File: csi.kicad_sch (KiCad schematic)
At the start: 61 parts, among them J10 Conn_FFC_WE_68715014522, J11 Conn_FFC_WE_68715014522, U43 PI4MSD5V9548AZDEX, U44 AP22615A_TSOT26, U45 AP22615A_TSOT26, U46 AP22615A_TSOT26, U47 AP22615A_TSOT26, U48 NTS0102_XSON, U49 NTS0102_XSON

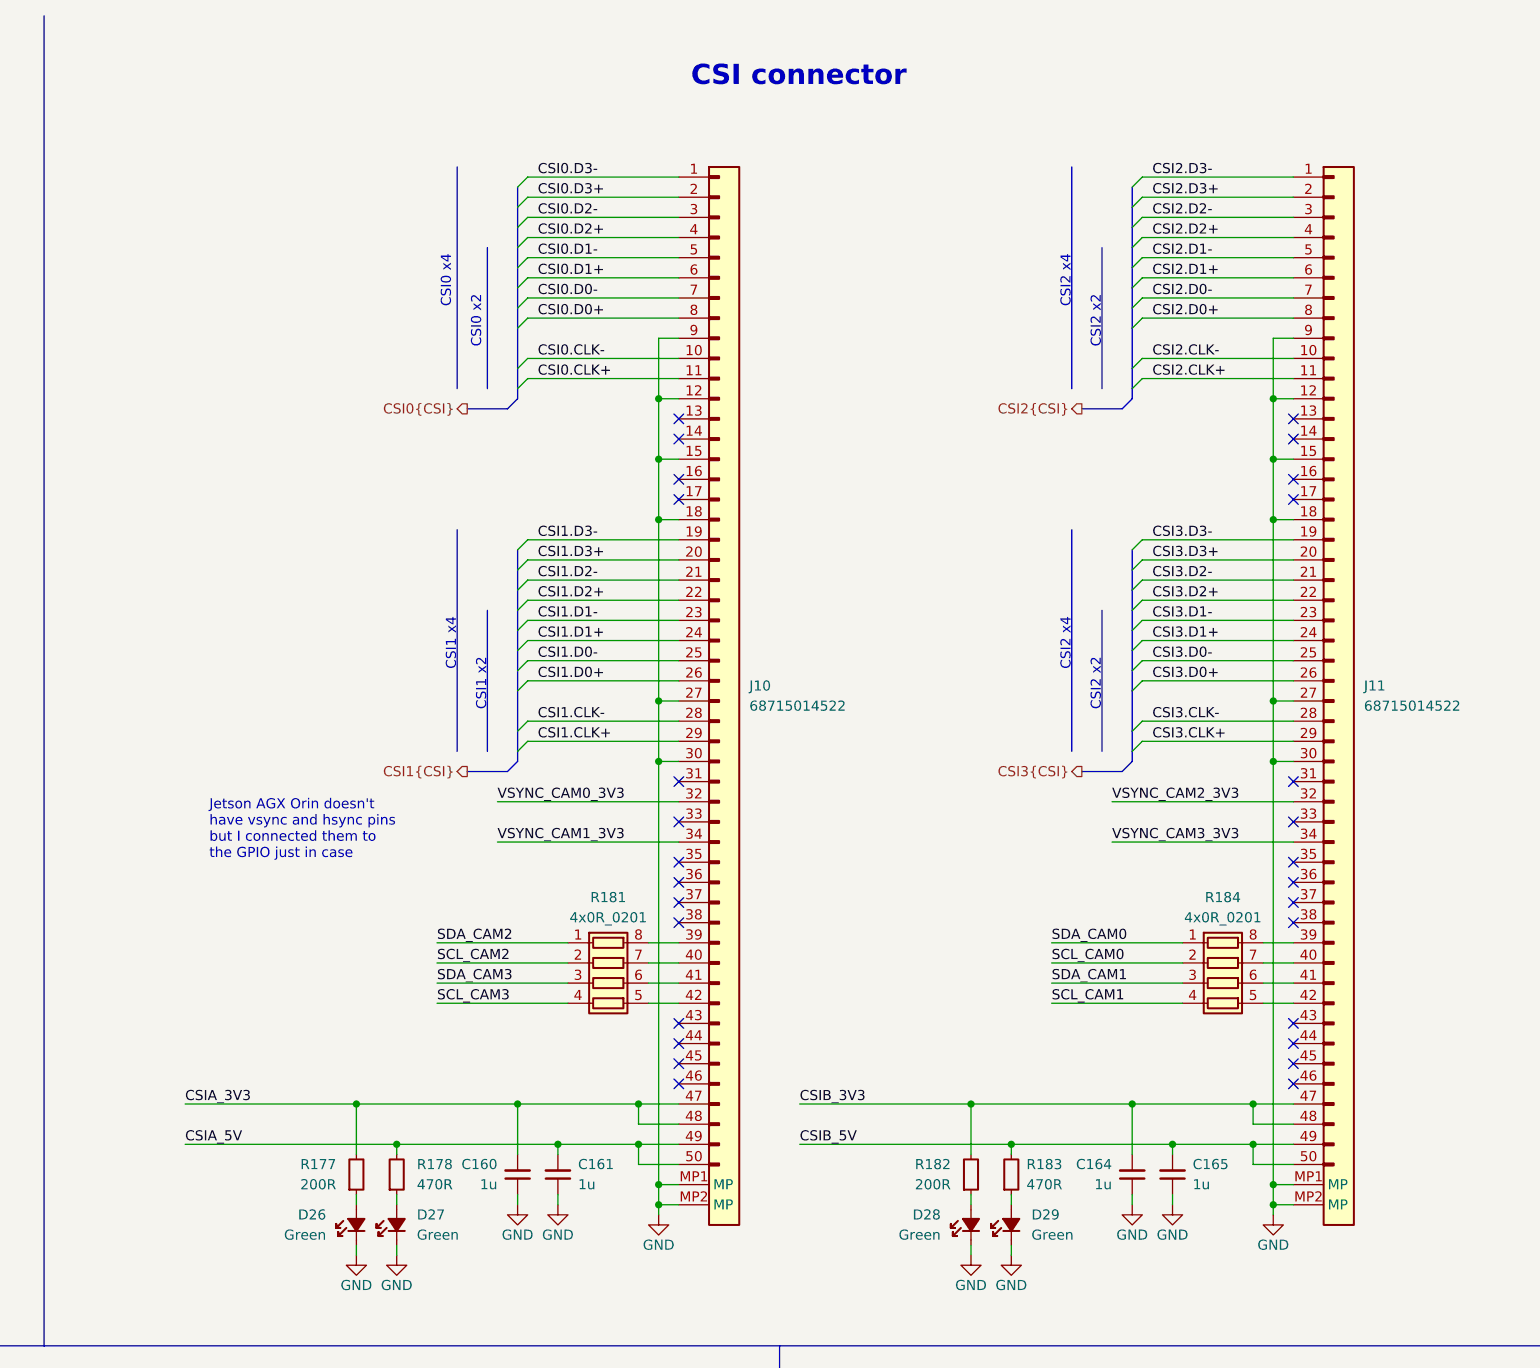
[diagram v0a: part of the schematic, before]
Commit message: [#83396] WIP: Route CSI - SoM to J11 connector
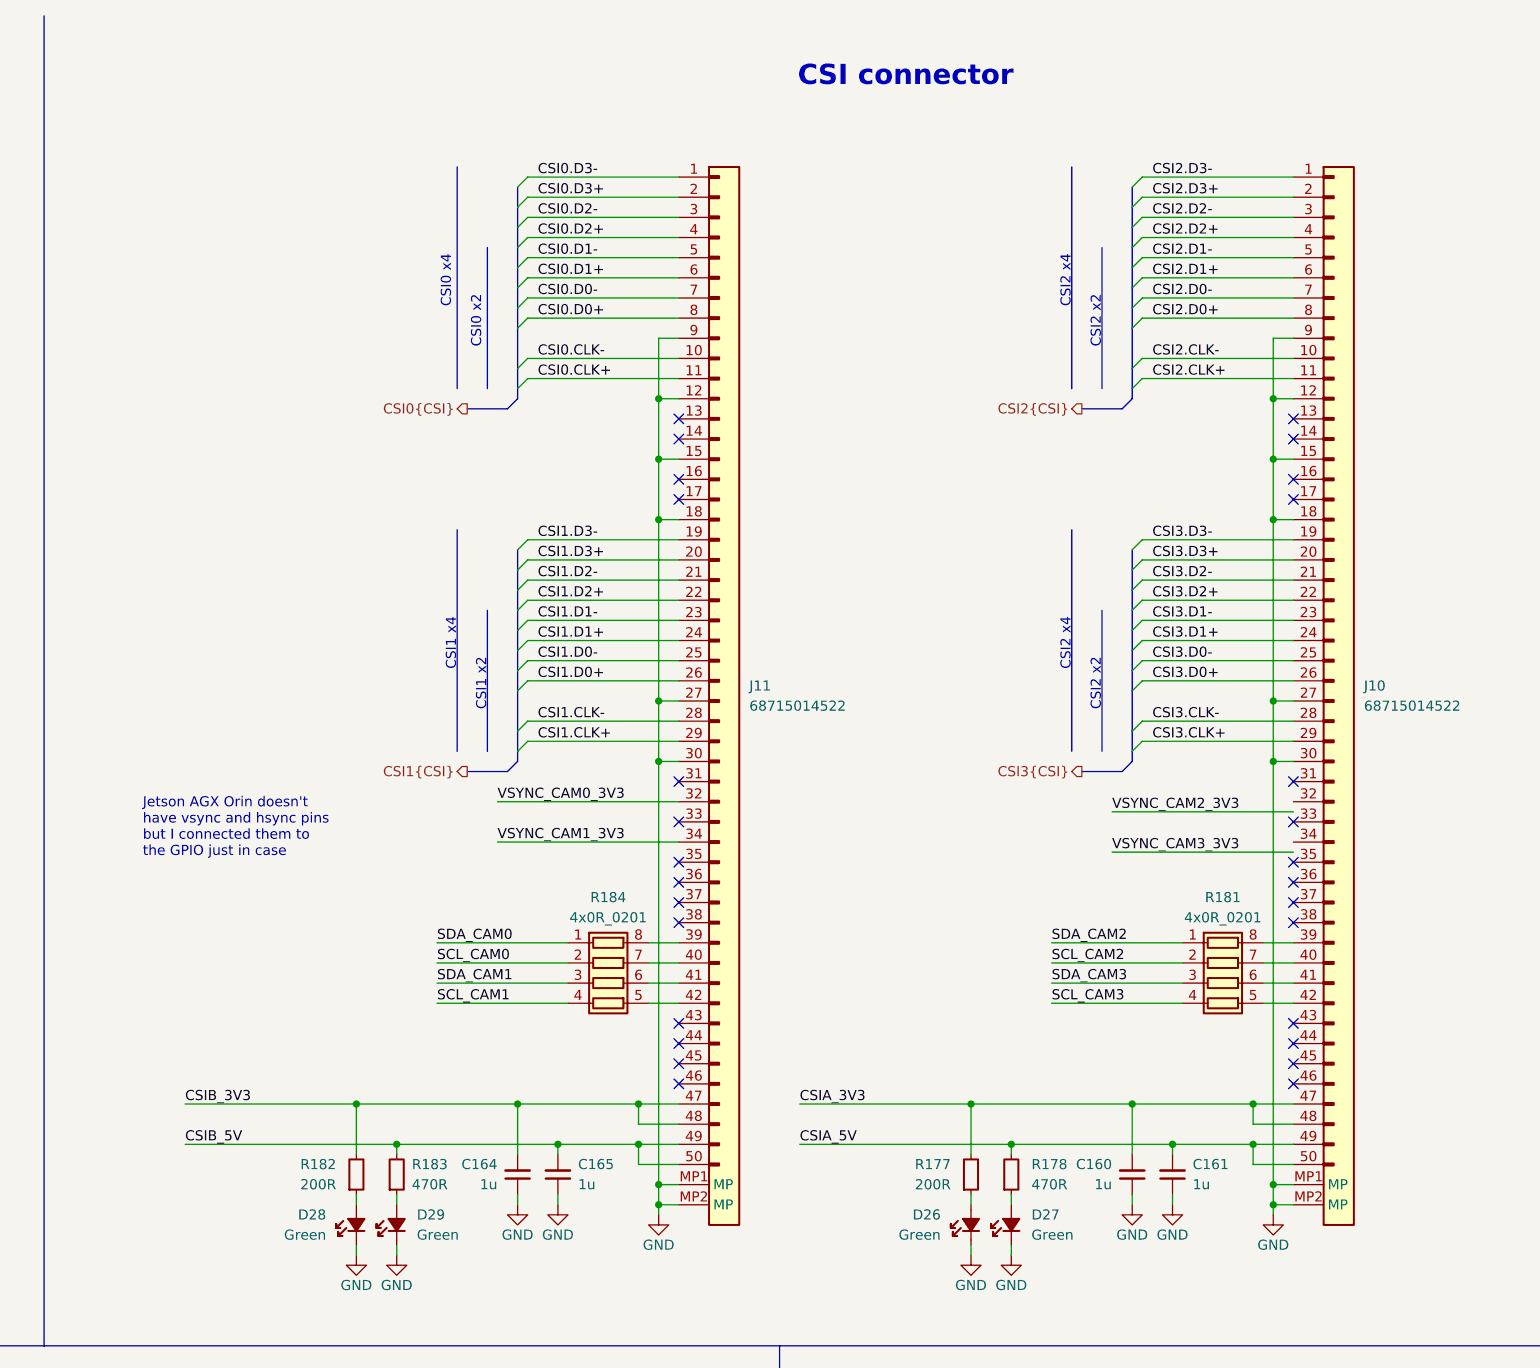
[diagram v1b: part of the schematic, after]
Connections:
- net CSI0.CLK+: now also J11.11; no longer J10.11
- net CSI0.CLK-: now also J11.10; no longer J10.10
- net CSI0.D0+: now also J11.8; no longer J10.8
- net CSI0.D0-: now also J11.7; no longer J10.7
- net CSI0.D1+: now also J11.6; no longer J10.6
- net CSI0.D1-: now also J11.5; no longer J10.5
- net CSI0.D2+: now also J11.4; no longer J10.4
- net CSI0.D2-: now also J11.3; no longer J10.3
- net CSI0.D3+: now also J11.2; no longer J10.2
- net CSI0.D3-: now also J11.1; no longer J10.1
- net CSI1.CLK+: now also J11.29; no longer J10.29
- net CSI1.CLK-: now also J11.28; no longer J10.28
- net CSI1.D0+: now also J11.26; no longer J10.26
- net CSI1.D0-: now also J11.25; no longer J10.25
- net CSI1.D1+: now also J11.24; no longer J10.24
- net CSI1.D1-: now also J11.23; no longer J10.23
- net CSI1.D2+: now also J11.22; no longer J10.22
- net CSI1.D2-: now also J11.21; no longer J10.21
- net CSI1.D3+: now also J11.20; no longer J10.20
- net CSI1.D3-: now also J11.19; no longer J10.19
- net CSI2.CLK+: now also J10.11; no longer J11.11
- net CSI2.CLK-: now also J10.10; no longer J11.10
- net CSI2.D0+: now also J10.8; no longer J11.8
- net CSI2.D0-: now also J10.7; no longer J11.7
- net CSI2.D1+: now also J10.6; no longer J11.6
- net CSI2.D1-: now also J10.5; no longer J11.5
- net CSI2.D2+: now also J10.4; no longer J11.4
- net CSI2.D2-: now also J10.3; no longer J11.3
- net CSI2.D3+: now also J10.2; no longer J11.2
- net CSI2.D3-: now also J10.1; no longer J11.1
- net CSI3.CLK+: now also J10.29; no longer J11.29
- net CSI3.CLK-: now also J10.28; no longer J11.28
- net CSI3.D0+: now also J10.26; no longer J11.26
- net CSI3.D0-: now also J10.25; no longer J11.25
- net CSI3.D1+: now also J10.24; no longer J11.24
- net CSI3.D1-: now also J10.23; no longer J11.23
- net CSI3.D2+: now also J10.22; no longer J11.22
- net CSI3.D2-: now also J10.21; no longer J11.21
- net CSI3.D3+: now also J10.20; no longer J11.20
- net CSI3.D3-: now also J10.19; no longer J11.19
- net VSYNC_CAM0_3V3: now also J11.32; no longer J10.32
- net VSYNC_CAM1_3V3: now also J11.34; no longer J10.34
- net VSYNC_CAM2_3V3: no longer J11.32
- net VSYNC_CAM3_3V3: no longer J11.34
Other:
- moved on the sheet: C160, C161, C164, C165, D26, D27, D28, D29, J10, J11, R177, R178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

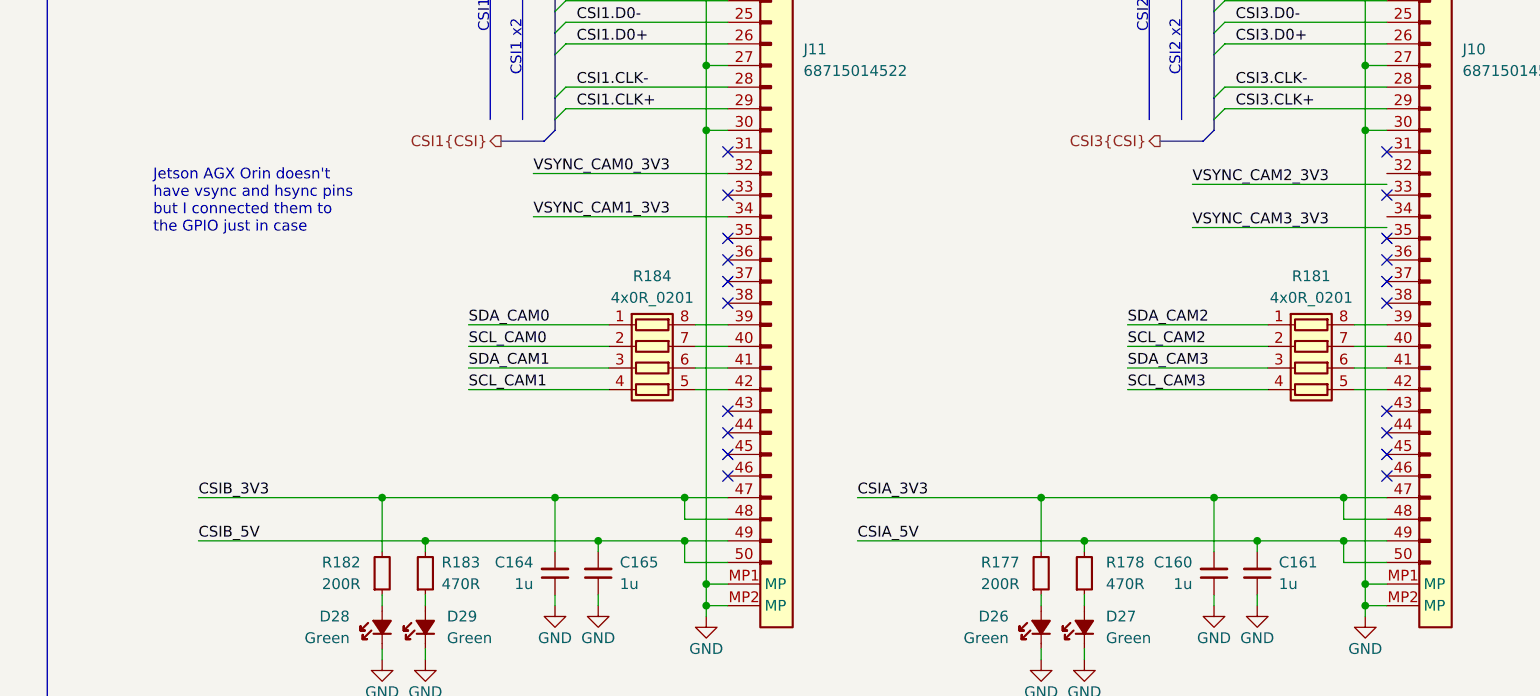
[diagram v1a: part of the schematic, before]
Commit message: [#83396] Update all symbols from library and clear all ERC errors
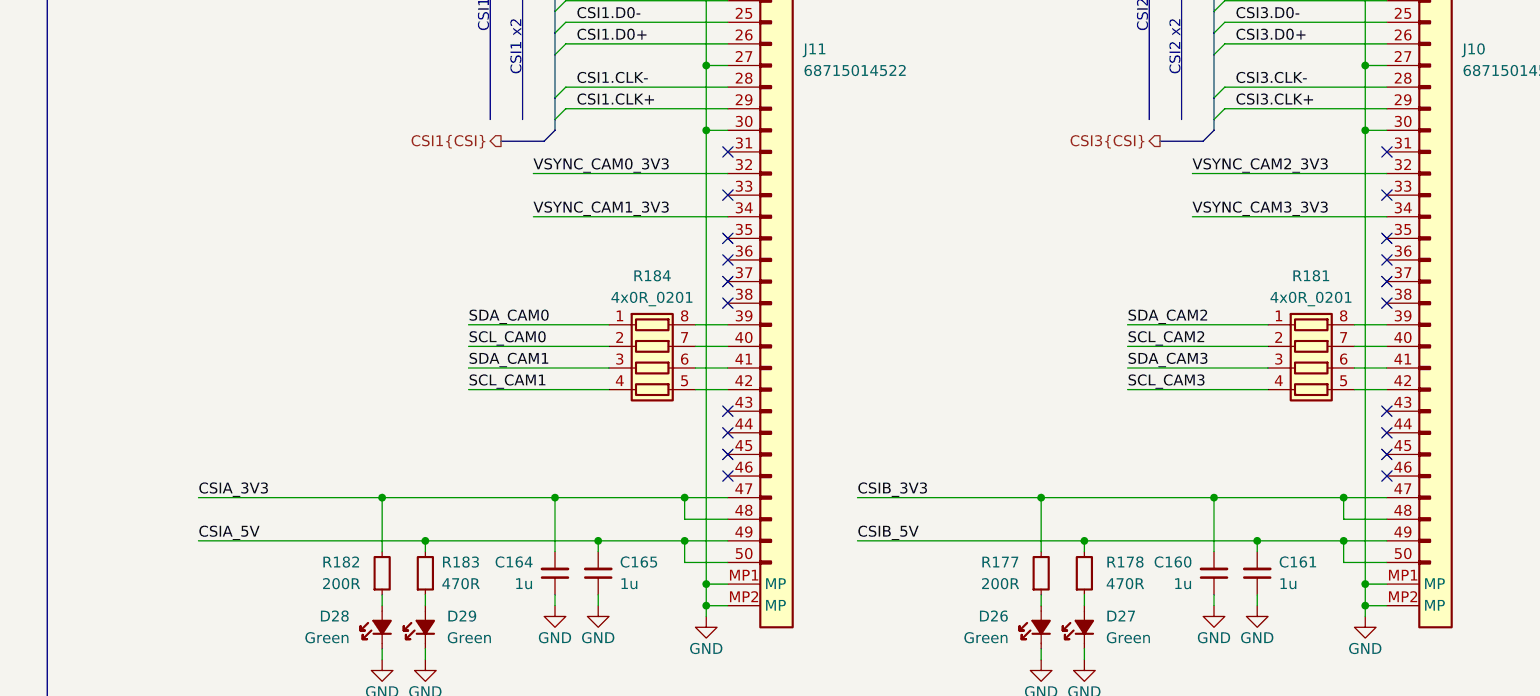
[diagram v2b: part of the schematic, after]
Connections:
- net CSIA_3V3: now also C164.2, J11.47, J11.48, R182.2; no longer C160.2, J10.47, J10.48, R177.2
- net CSIA_5V: now also C165.2, J11.49, J11.50, R183.2; no longer C161.2, J10.49, J10.50, R178.2
- net CSIB_3V3: now also C160.2, J10.47, J10.48, R177.2; no longer C164.2, J11.47, J11.48, R182.2
- net CSIB_5V: now also C161.2, J10.49, J10.50, R178.2; no longer C165.2, J11.49, J11.50, R183.2
- net VSYNC_CAM2_3V3: now also J10.32
- net VSYNC_CAM3_3V3: now also J10.34
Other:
- note removed: "Jetson AGX Orin doesn't have vsync and hsync pins but I connected them to the GPIO just in case"
